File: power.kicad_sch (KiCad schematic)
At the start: 10 parts, among them J20 Screw_Terminal_01x02, U6 AMS1117-3.3 SOT-223

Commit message: added gnd-radio and gnd-ant zones on two layers. ERC and DRC mostly good. (Two warnings about pads field in NetTie footprints.)
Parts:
- BT1: footprint ProjectLib:BatteryHolder_CR1220_SMT -> ProjectLib:BatteryHolder_LINX_BAT-HLD-012-SMT
- D3: footprint Package_TO_SOT_SMD:SOT-23 -> ProjectLib:SOT-23
- U6: footprint Package_TO_SOT_SMD:SOT-223-3_TabPin2 -> ProjectLib:SOT-223
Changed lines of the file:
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@@
 			)
 		)
-		(property "Footprint" "Package_TO_SOT_SMD:SOT-223-3_TabPin2"
+		(property "Footprint" "ProjectLib:SOT-223"
 			(at 152.4 92.71 0)
 			(hide yes)
@@
 			)
 		)
-		(property "Footprint" "ProjectLib:BatteryHolder_CR1220_SMT"
+		(property "Footprint" "ProjectLib:BatteryHolder_LINX_BAT-HLD-012-SMT"
 			(at 160.02 121.666 90)
 			(hide yes)
@@
 			)
 		)
-		(property "Datasheet" "HTTPS://www.batteryholders.com/uploads/parts/BC501SM/datasheets/BC501SM-datasheet.pdf"
+		(property "Datasheet" "https://www.te.com/commerce/DocumentDelivery/DDEController?Action=srchrtrv&DocNm=BAT-HLD-012-SMT&DocType=Data+Sheet&DocLang=English&DocFormat=pdf&PartCntxt=BAT-HLD-012-SMT"
 			(at 160.02 121.666 90)
 			(hide yes)
@@
 			)
 		)
-		(property "Footprint" "Package_TO_SOT_SMD:SOT-23"
+		(property "Footprint" "ProjectLib:SOT-23"
 			(at 146.685 121.285 0)
 			(hide yes)

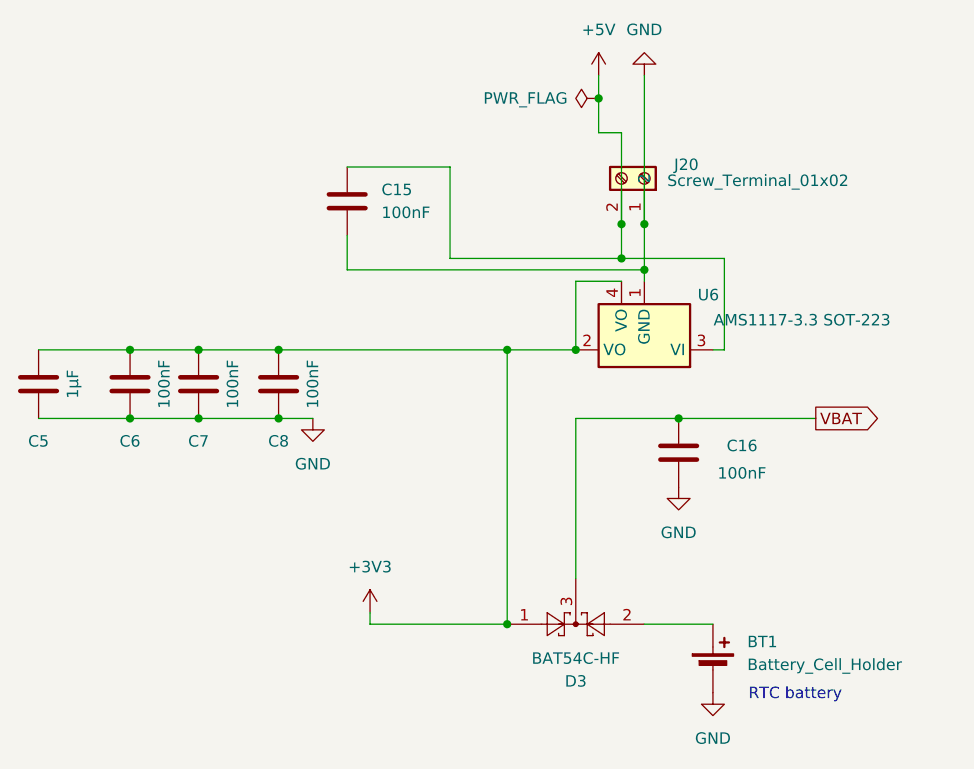
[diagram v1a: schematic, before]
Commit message: added QR and ID blocks on silkscreen. Marked HSE and LSE as DNP. Revised version number to 0.3.1.
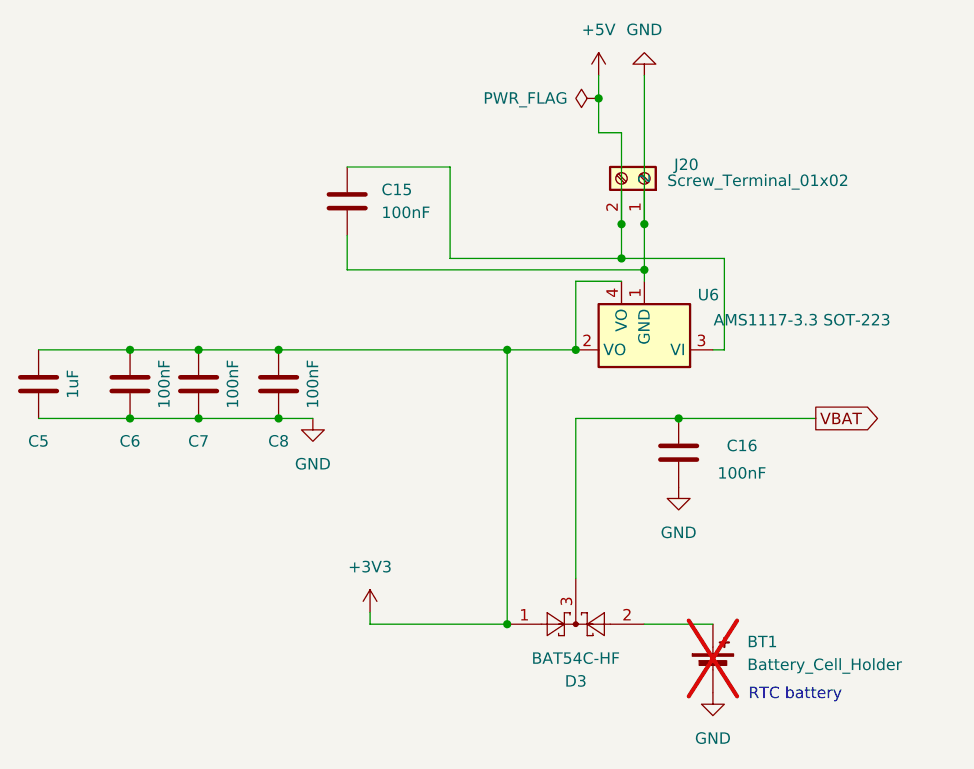
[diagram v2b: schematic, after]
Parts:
- BT1: now not fitted
- C5: value 1µF -> 1uF
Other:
- title: Power Regulator & RTC Battery -> stm32f411, RFM95W
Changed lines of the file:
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@@
 	(paper "A4")
 	(title_block
-		(title "Power Regulator & RTC Battery")
-		(date "2025-09-15")
-		(rev "v0.2.2")
+		(title "stm32f411, RFM95W")
+		(date "2026-04-12")
+		(rev "v0.3.1")
 	)
 	(text "RTC battery"
@@
 		(in_bom yes)
 		(on_board yes)
-		(in_pos_files yes)
-		(dnp no)
+		(in_pos_files no)
+		(dnp yes)
 		(property "Reference" "BT1"
 			(at 163.83 120.0784 0)
@@
 			)
 		)
-		(property "Value" "1µF"
+		(property "Value" "1uF"
 			(at 88.9 91.44 90)
 			(show_name no)
